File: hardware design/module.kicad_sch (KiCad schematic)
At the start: 85 parts, among them J10 JACK, J11 JACK, J12 JACK, J2 JACK, J4 JACK, J5 JACK, J6 JACK, J8 JACK, J9 JACK, Q3 MMBT3904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

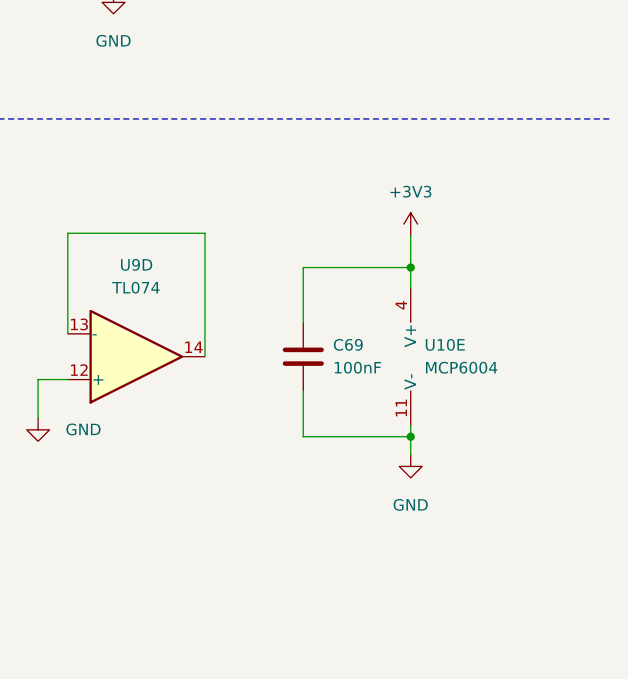
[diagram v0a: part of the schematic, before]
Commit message: redid power circuitry
5V is now switching regulator, separate LDO for analog and digital
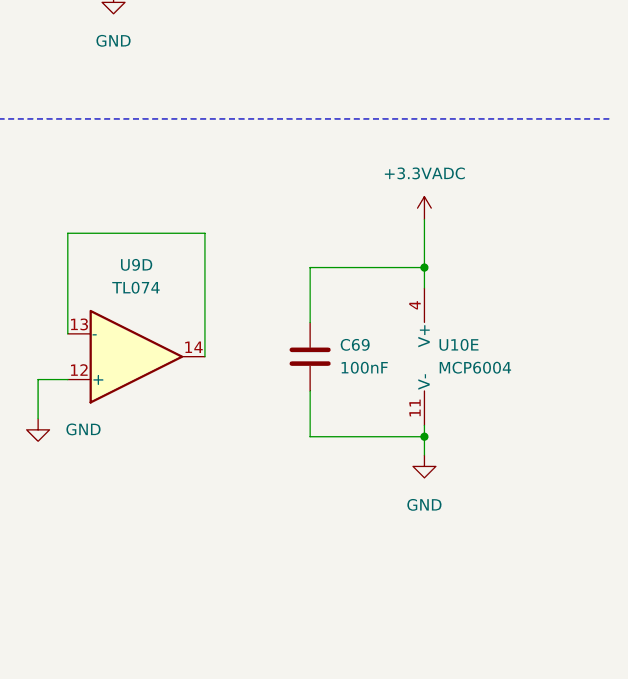
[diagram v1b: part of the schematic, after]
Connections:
- net +3V3: no longer C69.1, U10.4 (V+)
- new net +3.3VADC: C69.1, U10.4 (V+)
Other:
- moved on the sheet: C69, U10E
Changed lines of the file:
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@@
 	)
 	(junction
-		(at 385.826 225.044)
+		(at 387.35 225.044)
 		(diameter 0)
 		(color 0 0 0 0)
@@
 	)
 	(junction
-		(at 385.826 243.84)
+		(at 387.35 243.84)
 		(diameter 0)
 		(color 0 0 0 0)
@@
 	(wire
 		(pts
-			(xy 385.826 225.044) (xy 385.826 227.33)
+			(xy 387.35 225.044) (xy 387.35 227.33)
 		)
 		(stroke
@@
 	(wire
 		(pts
-			(xy 373.888 238.76) (xy 373.888 243.84)
+			(xy 374.65 238.76) (xy 374.65 243.84)
 		)
 		(stroke
@@
 	(wire
 		(pts
-			(xy 385.826 243.84) (xy 385.826 245.872)
+			(xy 387.35 243.84) (xy 387.35 245.872)
 		)
 		(stroke
@@
 	(wire
 		(pts
-			(xy 373.888 243.84) (xy 385.826 243.84)
+			(xy 374.65 243.84) (xy 387.35 243.84)
 		)
 		(stroke
@@
 	(wire
 		(pts
-			(xy 373.888 225.044) (xy 373.888 231.14)
+			(xy 374.65 225.044) (xy 374.65 231.14)
 		)
 		(stroke
@@
 	(wire
 		(pts
-			(xy 385.826 221.488) (xy 385.826 225.044)
+			(xy 387.35 219.71) (xy 387.35 225.044)
 		)
 		(stroke
@@
 	(wire
 		(pts
-			(xy 385.826 225.044) (xy 373.888 225.044)
+			(xy 387.35 225.044) (xy 374.65 225.044)
 		)
 		(stroke
@@
 	(wire
 		(pts
-			(xy 385.826 242.57) (xy 385.826 243.84)
+			(xy 387.35 242.57) (xy 387.35 243.84)
 		)
 		(stroke
@@
 	(symbol
 		(lib_id "Device:C")
-		(at 373.888 234.95 0)
+		(at 374.65 234.95 0)
 		(unit 1)
 		(exclude_from_sim no)
@@
 		(fields_autoplaced yes)
 		(property "Reference" "C69"
-			(at 377.19 233.6799 0)
+			(at 377.952 233.6799 0)
 			(effects
 				(font
@@
 		)
 		(property "Value" "100nF"
-			(at 377.19 236.2199 0)
+			(at 377.952 236.2199 0)
 			(effects
 				(font
@@
 		)
 		(property "Footprint" "Capacitor_SMD:C_0603_1608Metric"
-			(at 374.8532 238.76 0)
+			(at 375.6152 238.76 0)
 			(effects
 				(font
@@
 		)
 		(property "Datasheet" "~"
-			(at 373.888 234.95 0)
+			(at 374.65 234.95 0)
 			(effects
 				(font
@@
 		)
 		(property "Description" ""
-			(at 373.888 234.95 0)
+			(at 374.65 234.95 0)
 			(effects
 				(font
@@
 	(symbol
 		(lib_id "Amplifier_Operational:MCP6004")
-		(at 388.366 234.95 0)
+		(at 389.89 234.95 0)
 		(unit 5)
 		(exclude_from_sim no)
@@
 		(fields_autoplaced yes)
 		(property "Reference" "U10"
-			(at 387.35 233.6799 0)
+			(at 388.874 233.6799 0)
 			(effects
 				(font
@@
 		)
 		(property "Value" "MCP6004"
-			(at 387.35 236.2199 0)
+			(at 388.874 236.2199 0)
 			(effects
 				(font
@@
 		)
 		(property "Footprint" "Package_SO:SOIC-14_3.9x8.7mm_P1.27mm"
-			(at 387.096 232.41 0)
+			(at 388.62 232.41 0)
 			(effects
 				(font
@@
 		)
 		(property "Datasheet" "http://ww1.microchip.com/downloads/en/DeviceDoc/21733j.pdf"
-			(at 389.636 229.87 0)
+			(at 391.16 229.87 0)
 			(effects
 				(font
@@
 		)
 		(property "Description" ""
-			(at 388.366 234.95 0)
+			(at 389.89 234.95 0)
 			(effects
 				(font
@@
 	)
 	(symbol
-		(lib_id "power:+3V3")
-		(at 385.826 221.488 0)
-		(unit 1)
-		(exclude_from_sim no)
-		(in_bom yes)
-		(on_board yes)
-		(dnp no)
-		(fields_autoplaced yes)
-		(property "Reference" "#PWR0211"
-			(at 385.826 225.298 0)
-			(effects
-				(font
-					(size 1.27 1.27)
-				)
-				(hide yes)
-			)
-		)
-		(property "Value" "+3V3"
-			(at 385.826 216.662 0)
-			(effects
-				(font
-					(size 1.27 1.27)
-				)
-			)
-		)
-		(property "Footprint" ""
-			(at 385.826 221.488 0)
-			(effects
-				(font
-					(size 1.27 1.27)
-				)
-				(hide yes)
-			)
-		)
-		(property "Datasheet" ""
-			(at 385.826 221.488 0)
-			(effects
-				(font
-					(size 1.27 1.27)
-				)
-				(hide yes)
-			)
-		)
-		(property "Description" ""
-			(at 385.826 221.488 0)
-			(effects
-				(font
-					(size 1.27 1.27)
-				)
-				(hide yes)
-			)
-		)
-		(pin "1"
-		)
-		(instances
-			(project "dsug_cctv_BOARD"
-				(path "/51d56f2e-5cbb-4b7a-b5cc-91fdc3a7308d/01856007-427f-4a2f-8b02-0471af5a1061"
-					(reference "#PWR0211")
-					(unit 1)
-				)
-				(path "/51d56f2e-5cbb-4b7a-b5cc-91fdc3a7308d/bd8c531c-02a8-4190-9c59-8241bb2368bf"
-					(reference "#PWR0148")
-					(unit 1)
-				)
-			)
-		)
-	)
-	(symbol
 		(lib_id "Device:R_US")
 		(at 44.45 161.798 90)
@@
 	)
 	(symbol
+		(lib_id "power:+3.3VADC")
+		(at 387.35 219.71 0)
+		(unit 1)
+		(exclude_from_sim no)
+		(in_bom yes)
+		(on_board yes)
+		(dnp no)
+		(fields_autoplaced yes)
+		(property "Reference" "#PWR0191"
+			(at 391.16 220.98 0)
+			(effects
+				(font
+					(size 1.27 1.27)
+				)
+				(hide yes)
+			)
+		)
+		(property "Value" "+3.3VADC"
+			(at 387.35 214.63 0)
+			(effects
+				(font
+					(size 1.27 1.27)
+				)
+			)
+		)
+		(property "Footprint" ""
+			(at 387.35 219.71 0)
+			(effects
+				(font
+					(size 1.27 1.27)
+				)
+				(hide yes)
+			)
+		)
+		(property "Datasheet" ""
+			(at 387.35 219.71 0)
+			(effects
+				(font
+					(size 1.27 1.27)
+				)
+				(hide yes)
+			)
+		)
+		(property "Description" "Power symbol creates a global label with name \"+3.3VADC\""
+			(at 387.35 219.71 0)
+			(effects
+				(font
+					(size 1.27 1.27)
+				)
+				(hide yes)
+			)
+		)
+		(pin "1"
+		)
+		(instances
+			(project "dsug_cctv_BOARD"
+				(path "/51d56f2e-5cbb-4b7a-b5cc-91fdc3a7308d/bd8c531c-02a8-4190-9c59-8241bb2368bf"
+					(reference "#PWR0191")
+					(unit 1)
+				)
+				(path "/51d56f2e-5cbb-4b7a-b5cc-91fdc3a7308d/01856007-427f-4a2f-8b02-0471af5a1061"
+					(reference "#PWR0148")
+					(unit 1)
+				)
+			)
+		)
+	)
+	(symbol
 		(lib_id "power:GND")
 		(at 218.186 266.7 0)
@@
 	(symbol
 		(lib_id "power:GND")
-		(at 385.826 245.872 0)
+		(at 387.35 245.872 0)
 		(unit 1)
 		(exclude_from_sim no)
@@
 		(fields_autoplaced yes)
 		(property "Reference" "#PWR0212"
-			(at 385.826 252.222 0)
+			(at 387.35 252.222 0)
 			(effects
 				(font
@@
 		)
 		(property "Value" "GND"
-			(at 385.826 251.46 0)
+			(at 387.35 251.46 0)
 			(effects
 				(font
@@
 		)
 		(property "Footprint" ""
-			(at 385.826 245.872 0)
+			(at 387.35 245.872 0)
 			(effects
 				(font
@@
 		)
 		(property "Datasheet" ""
-			(at 385.826 245.872 0)
+			(at 387.35 245.872 0)
 			(effects
 				(font
@@
 		)
 		(property "Description" ""
-			(at 385.826 245.872 0)
+			(at 387.35 245.872 0)
 			(effects
 				(font

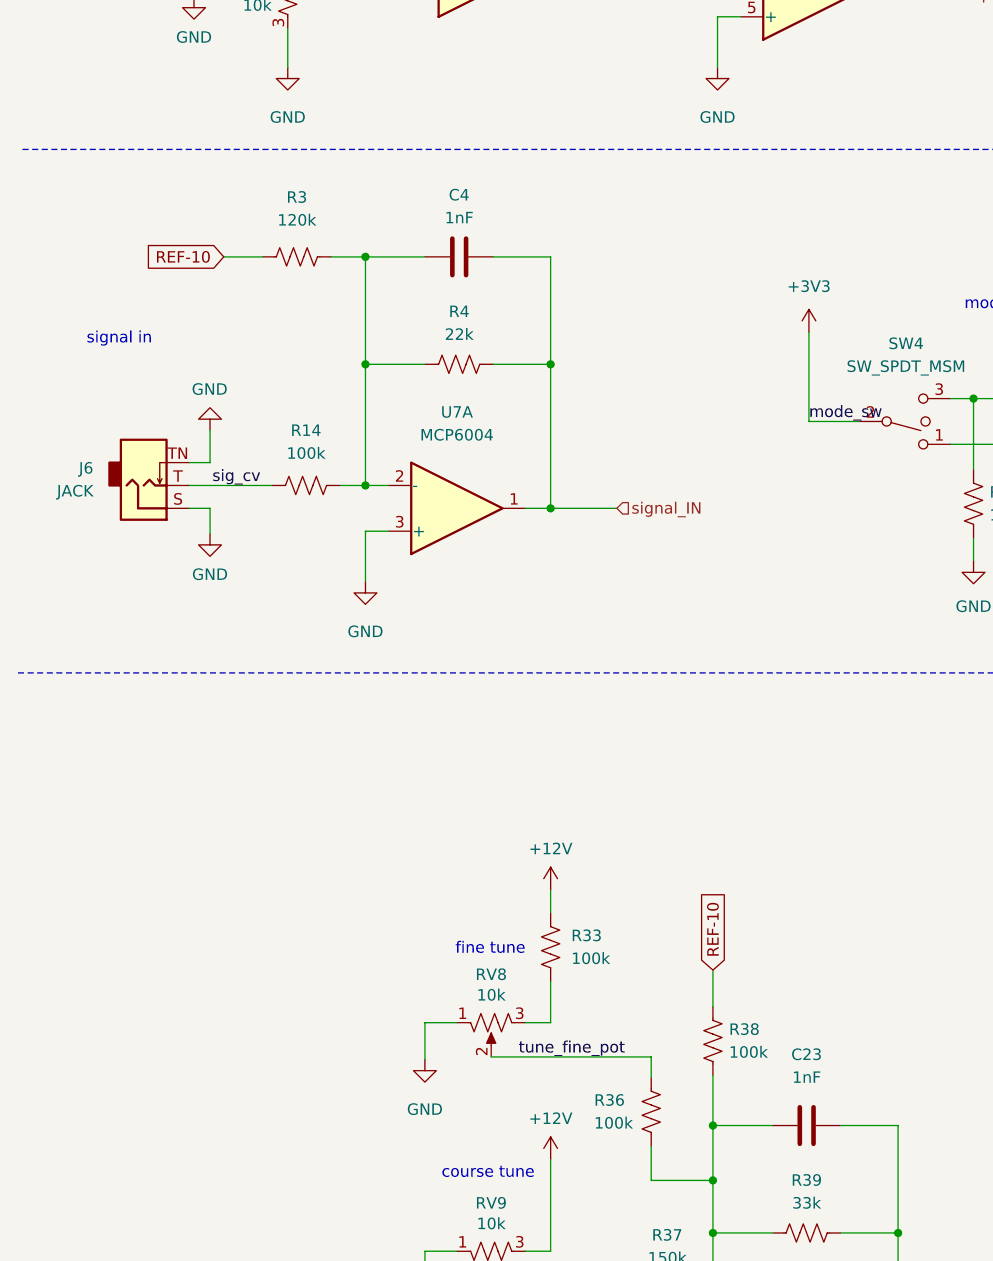
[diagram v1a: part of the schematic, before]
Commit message: minor changes
switched caps on V/O input, changed resistors for trig in
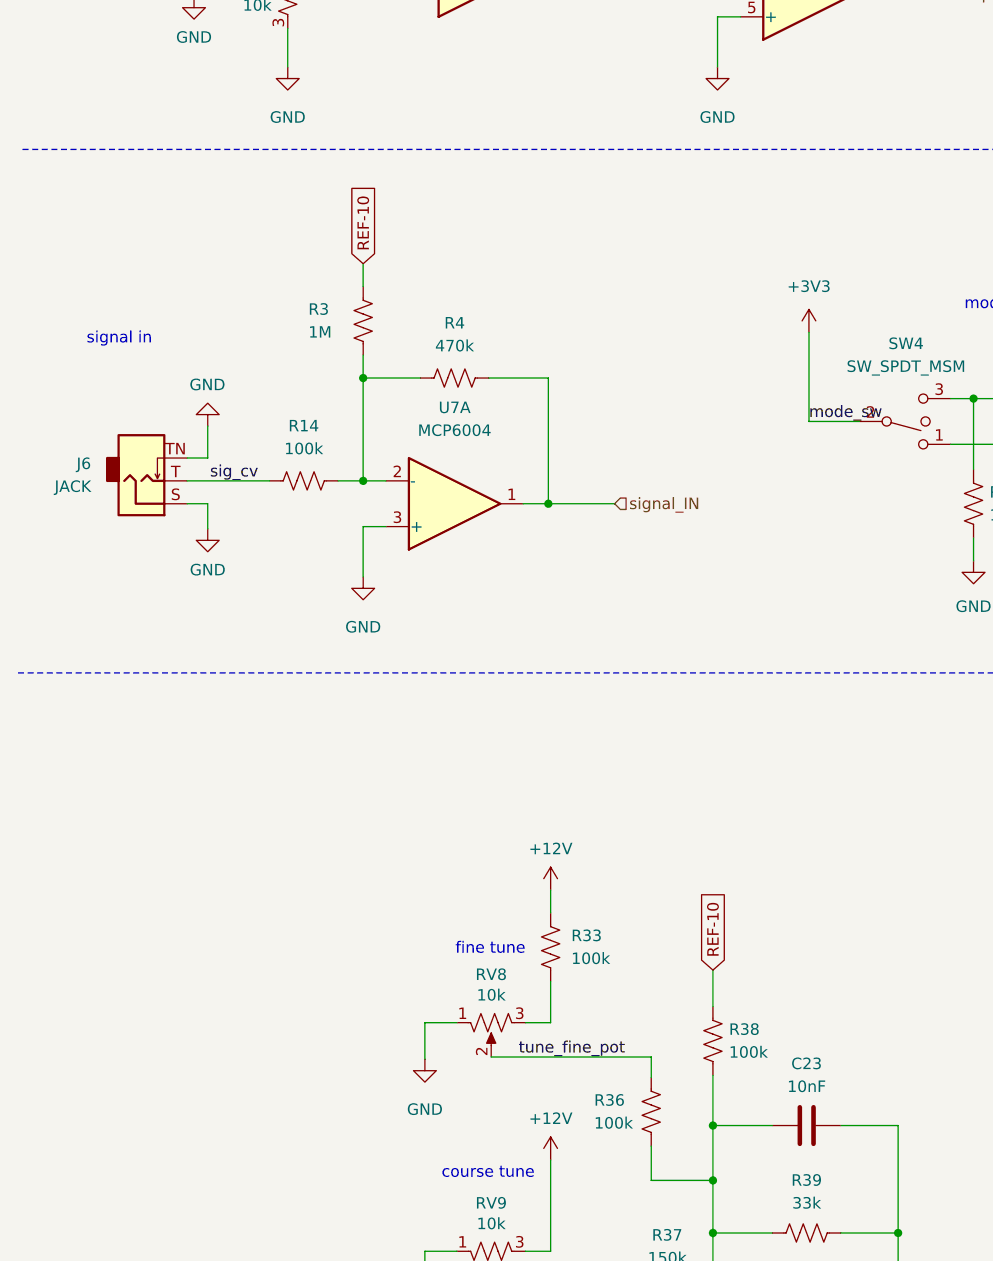
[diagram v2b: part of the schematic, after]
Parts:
- removed C4: 1nF, Capacitor_SMD:C_0603_1608Metric, symbol Device:C
- C23: value 1nF -> 10nF
- R3: value 120k -> 1M
- R4: value 22k -> 470k
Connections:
- net REF-10: now also R3.2; no longer R3.1
- net at R14.2, R4.1, U7.2 (-): now also R3.1; no longer R3.2
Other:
- moved on the sheet: J6, R14, R3, R4, U7A

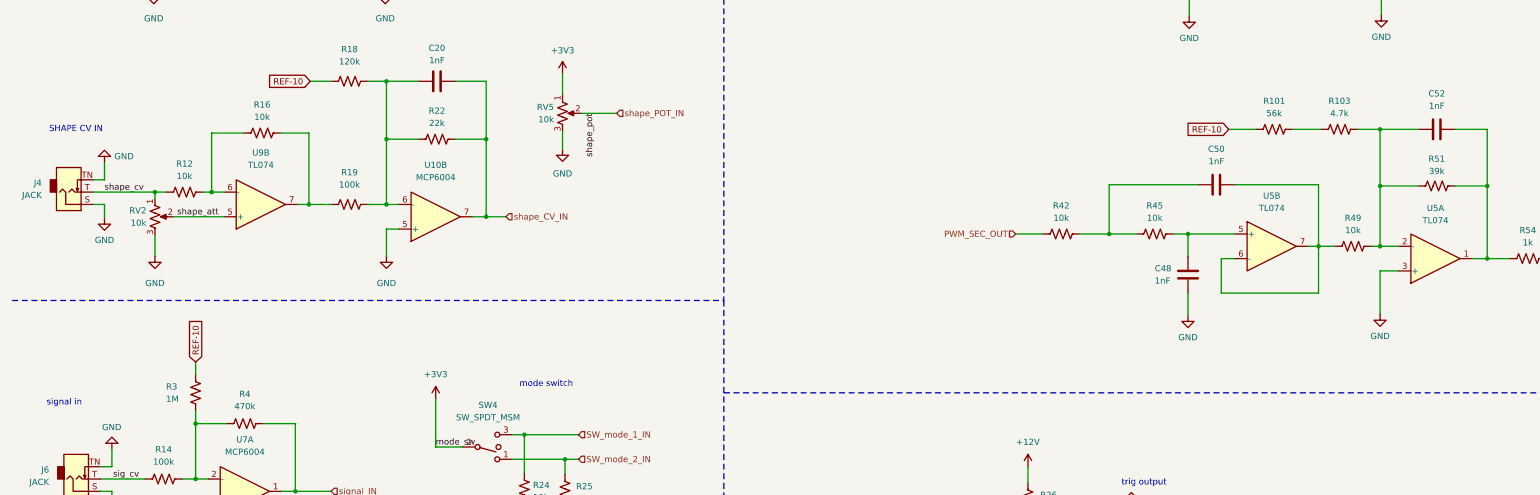
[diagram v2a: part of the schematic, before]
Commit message: fixing schematic issues, change output caps
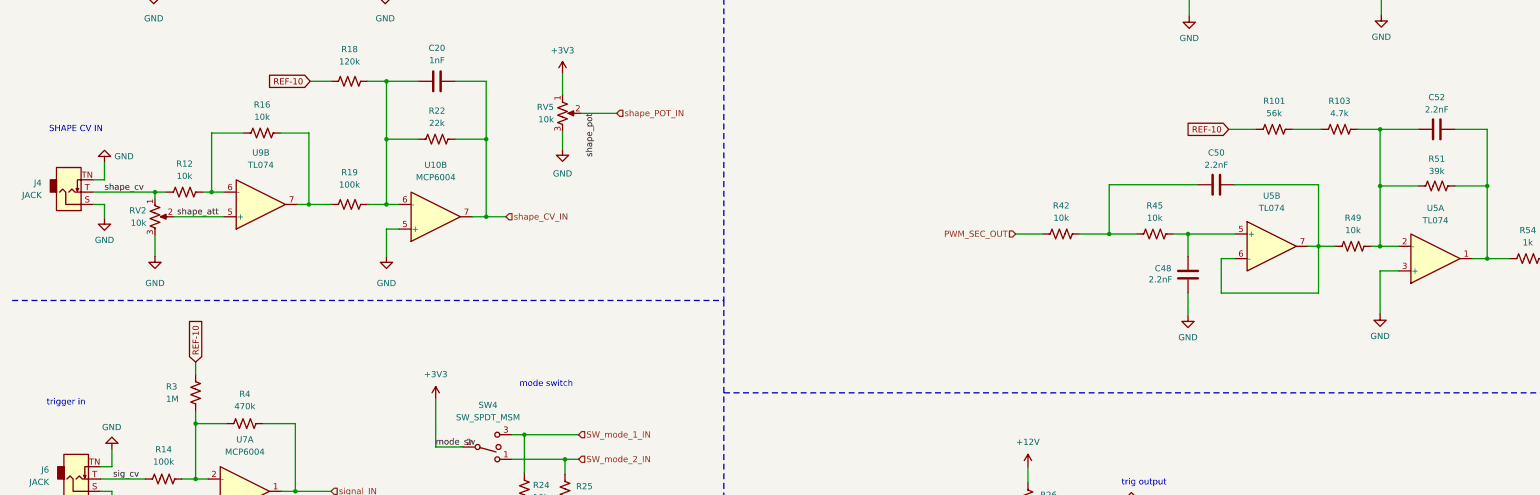
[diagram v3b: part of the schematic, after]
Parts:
- C48, C50, C52: value 1nF -> 2.2nF
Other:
- note added: "trigger in"
- note removed: "signal in"
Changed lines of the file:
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@@
 		)
 	)
-	(text "signal in"
+	(text "trigger in"
 		(exclude_from_sim no)
 		(at 20.066 146.304 0)
@@
 		(fields_autoplaced yes)
 		(property "Reference" "C50"
-			(at 261.366 93.218 90)
+			(at 261.366 93.98 90)
 			(effects
 				(font
@@
 			)
 		)
-		(property "Value" "1nF"
-			(at 261.366 95.758 90)
+		(property "Value" "2.2nF"
+			(at 261.366 96.52 90)
 			(effects
 				(font
@@
 		(fields_autoplaced yes)
 		(property "Reference" "C52"
-			(at 306.832 81.788 90)
+			(at 306.832 82.55 90)
 			(effects
 				(font
@@
 			)
 		)
-		(property "Value" "1nF"
-			(at 306.832 84.328 90)
+		(property "Value" "2.2nF"
+			(at 306.832 85.09 90)
 			(effects
 				(font
@@
 			)
 		)
-		(property "Value" "1nF"
-			(at 248.666 120.396 0)
+		(property "Value" "2.2nF"
+			(at 247.396 120.142 0)
 			(effects
 				(font

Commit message: pcb rev2.5
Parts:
- R33, R38: value 100k -> 180k
- R36: value 100k -> 120k
- R37: value 150k -> 270k
- R39: value 33k -> 47k
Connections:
- net +3.3VADC: now also RV4.1, RV5.1
- net +3V3: no longer RV4.1, RV5.1
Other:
- moved on the sheet: RV4, RV5

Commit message: minor pcb changes
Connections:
- net trig_OUT renamed TRIG_OUT
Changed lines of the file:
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@@
 		)
 	)
-	(hierarchical_label "trig_OUT"
+	(hierarchical_label "TRIG_OUT"
 		(shape input)
 		(at 198.882 180.848 180)

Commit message: library name updating, footprint swaps
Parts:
- J10, J11, J12, J2, J4, J5, J6, J8, J9: footprint EURORACK:AudioJack_3.5mm_with_drawing -> benjiaomodular:AudioJack_3.5mm_with_drawing
- RV2, RV3, RV7, RV8: footprint EURORACK:Potentiometer_RV09_talltrimmer -> benjiaomodular:Potentiometer_RV09_talltrimmer
- RV4, RV5, RV9: footprint EURORACK:Potentiometer_RV09_6mm_knob -> benjiaomodular:Potentiometer_RV09_6mm_knob
- SW4: footprint EURORACK:SPDT_P2.54mm_Vertical -> benjiaomodular:SPDT_P2.54mm_Vertical
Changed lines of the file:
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@@
 			)
 		)
-		(property "Footprint" "EURORACK:Potentiometer_RV09_6mm_knob"
+		(property "Footprint" "benjiaomodular:Potentiometer_RV09_6mm_knob"
 			(at 65.024 246.888 0)
 			(effects
@@
 			)
 		)
-		(property "Footprint" "EURORACK:SPDT_P2.54mm_Vertical"
+		(property "Footprint" "benjiaomodular:SPDT_P2.54mm_Vertical"
 			(at 110.998 154.686 0)
 			(effects
@@
 			)
 		)
-		(property "Footprint" "EURORACK:AudioJack_3.5mm_with_drawing"
+		(property "Footprint" "benjiaomodular:AudioJack_3.5mm_with_drawing"
 			(at 26.162 161.29 0)
 			(effects
@@
 			)
 		)
-		(property "Footprint" "EURORACK:Potentiometer_RV09_talltrimmer"
+		(property "Footprint" "benjiaomodular:Potentiometer_RV09_talltrimmer"
 			(at 42.418 107.188 0)
 			(effects
@@
 			)
 		)
-		(property "Footprint" "EURORACK:AudioJack_3.5mm_with_drawing"
+		(property "Footprint" "benjiaomodular:AudioJack_3.5mm_with_drawing"
 			(at 40.894 258.318 0)
 			(effects
@@
 			)
 		)
-		(property "Footprint" "EURORACK:AudioJack_3.5mm_with_drawing"
+		(property "Footprint" "benjiaomodular:AudioJack_3.5mm_with_drawing"
 			(at 24.638 102.108 0)
 			(effects
@@
 			)
 		)
-		(property "Footprint" "EURORACK:AudioJack_3.5mm_with_drawing"
+		(property "Footprint" "benjiaomodular:AudioJack_3.5mm_with_drawing"
 			(at 290.068 181.102 0)
 			(effects
@@
 			)
 		)
-		(property "Footprint" "EURORACK:Potentiometer_RV09_talltrimmer"
+		(property "Footprint" "benjiaomodular:Potentiometer_RV09_talltrimmer"
 			(at 307.848 186.182 0)
 			(effects
@@
 			)
 		)
-		(property "Footprint" "EURORACK:AudioJack_3.5mm_with_drawing"
+		(property "Footprint" "benjiaomodular:AudioJack_3.5mm_with_drawing"
 			(at 343.154 54.102 0)
 			(effects
@@
 			)
 		)
-		(property "Footprint" "EURORACK:Potentiometer_RV09_6mm_knob"
+		(property "Footprint" "benjiaomodular:Potentiometer_RV09_6mm_knob"
 			(at 127 29.21 0)
 			(effects
@@
 			)
 		)
-		(property "Footprint" "EURORACK:AudioJack_3.5mm_with_drawing"
+		(property "Footprint" "benjiaomodular:AudioJack_3.5mm_with_drawing"
 			(at 24.384 47.498 0)
 			(effects
@@
 			)
 		)
-		(property "Footprint" "EURORACK:AudioJack_3.5mm_with_drawing"
+		(property "Footprint" "benjiaomodular:AudioJack_3.5mm_with_drawing"
 			(at 188.976 256.032 0)
 			(effects
@@
 			)
 		)
-		(property "Footprint" "EURORACK:Potentiometer_RV09_talltrimmer"
+		(property "Footprint" "benjiaomodular:Potentiometer_RV09_talltrimmer"
 			(at 42.164 52.578 0)
 			(effects
@@
 			)
 		)
-		(property "Footprint" "EURORACK:Potentiometer_RV09_6mm_knob"
+		(property "Footprint" "benjiaomodular:Potentiometer_RV09_6mm_knob"
 			(at 127 85.09 0)
 			(effects
@@
 			)
 		)
-		(property "Footprint" "EURORACK:Potentiometer_RV09_talltrimmer"
+		(property "Footprint" "benjiaomodular:Potentiometer_RV09_talltrimmer"
 			(at 65.024 221.488 0)
 			(effects
@@
 			)
 		)
-		(property "Footprint" "EURORACK:AudioJack_3.5mm_with_drawing"
+		(property "Footprint" "benjiaomodular:AudioJack_3.5mm_with_drawing"
 			(at 342.9 115.824 0)
 			(effects
@@
 			)
 		)
-		(property "Footprint" "EURORACK:AudioJack_3.5mm_with_drawing"
+		(property "Footprint" "benjiaomodular:AudioJack_3.5mm_with_drawing"
 			(at 251.206 172.72 0)
 			(effects
